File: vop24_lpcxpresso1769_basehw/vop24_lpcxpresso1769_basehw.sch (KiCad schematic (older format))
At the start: 33 parts

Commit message: Esquematico:    - se paso el circuito de fuentes a una hoja aparte    - falta pasar todas las demas a hojas separadas    - terminar conexiones del ads    - poner desacoples de alimentacion para cada IC    - ver como agregar texto para las recomendaciones de ruteo
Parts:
- removed C? (x4): C_Small, symbol C_Small
- removed D? (x2): LED_Small, symbol LED_Small
- removed J?: Conn_01x02, symbol Conn_01x02
- removed R? (x4): R_Small, symbol R_Small
- removed U? (x2): MCP1700T-3302E_TT, digikey-footprints:SOT-23-3, symbol MCP1700T-3302E_TT
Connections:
- net labels removed: VBAT, VREFN
- wire segments 124 -> 101

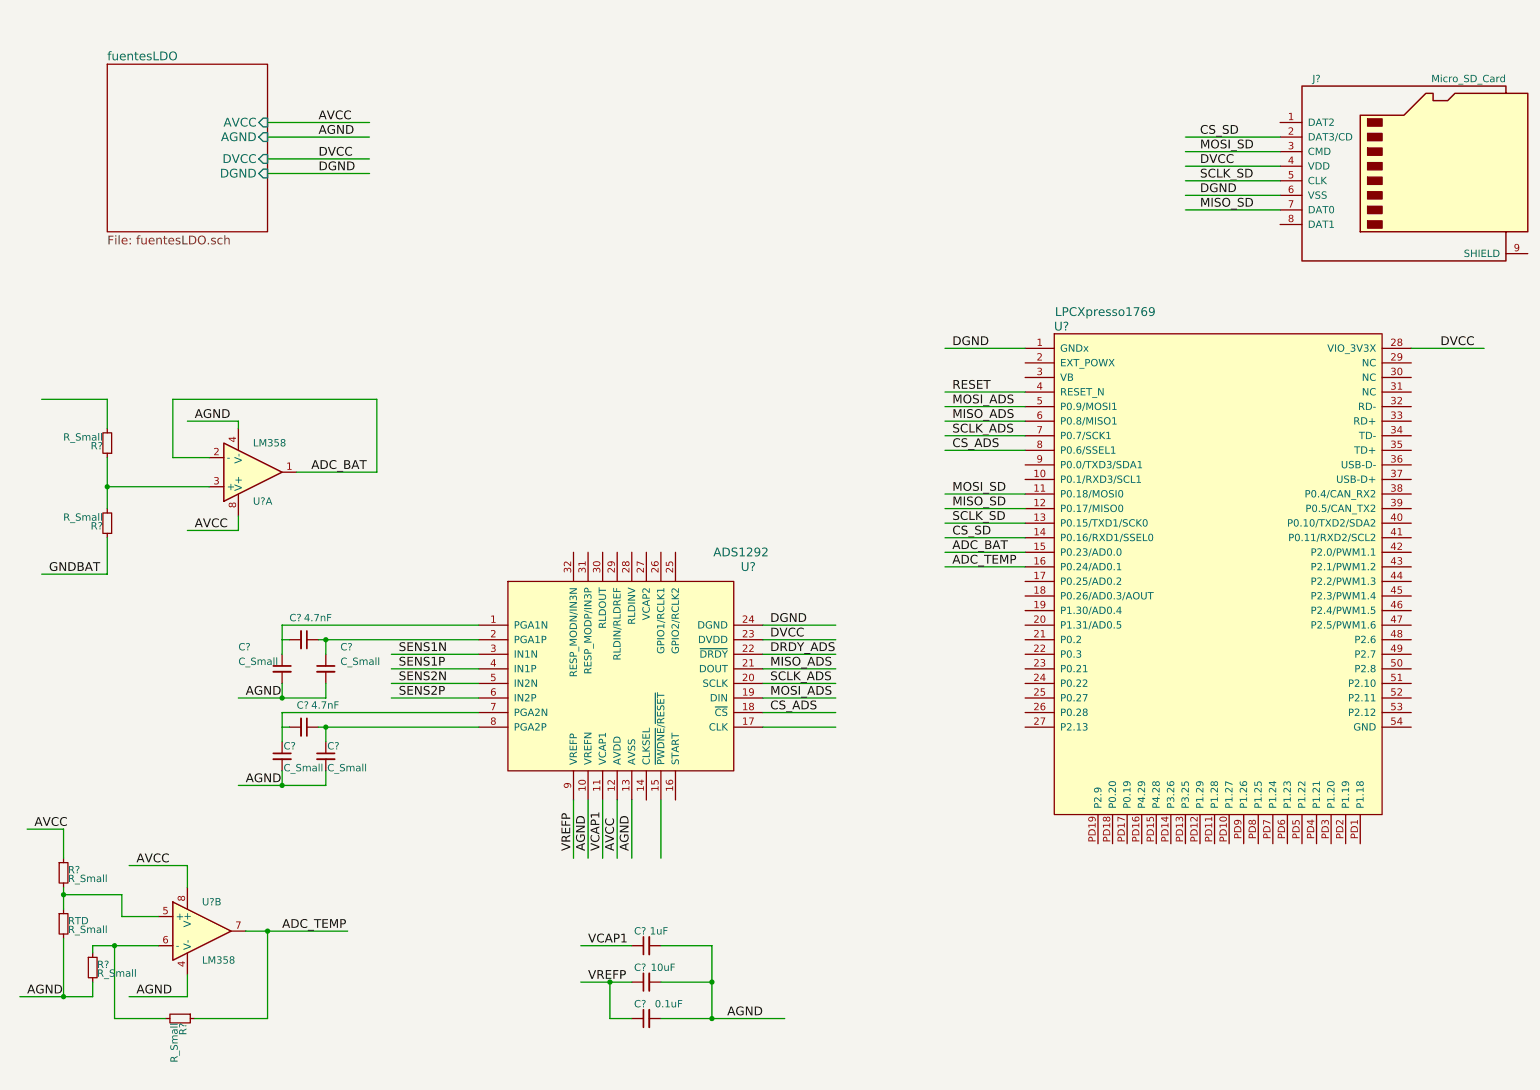
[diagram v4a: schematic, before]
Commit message: Esquematico: agregados hojas separadas de entradas analogicas terminadas y ads1292 sin terminar
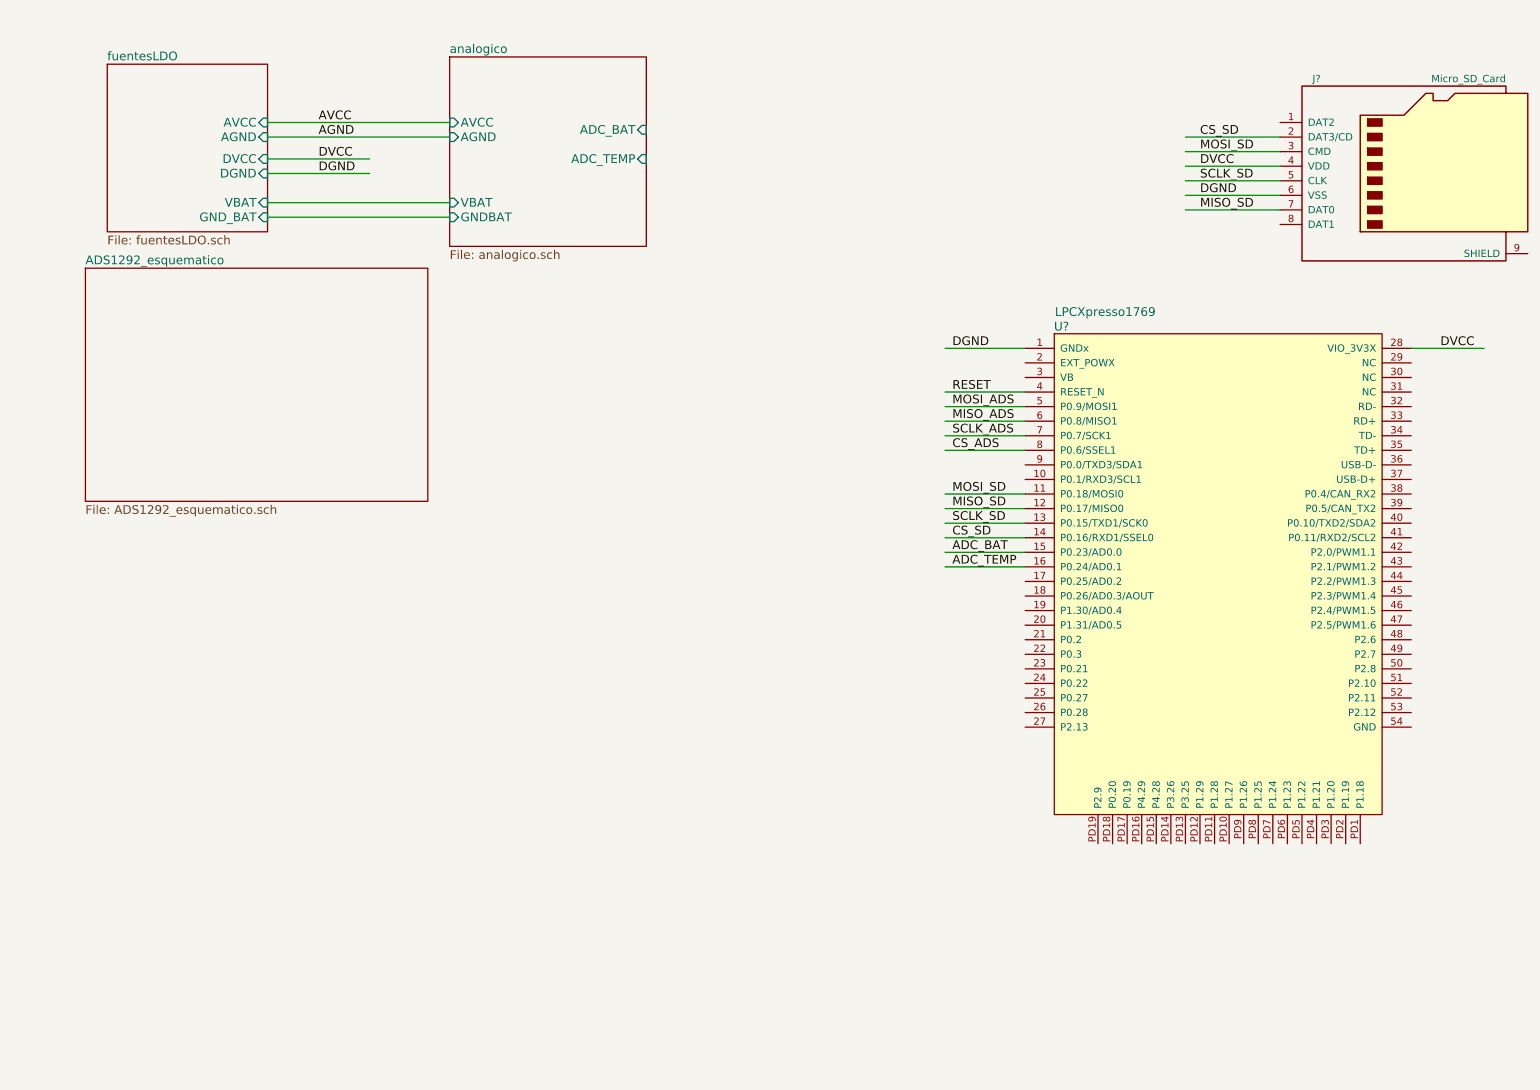
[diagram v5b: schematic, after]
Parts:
- removed C? (x4): C_Small, symbol C_Small
- removed C? (x2): 4.7nF, symbol C_Small
- removed C?: 1uF, symbol C_Small
- removed C?: 10uF, symbol C_Small
- removed C?: 0.1uF, symbol C_Small
- removed R? (x5), RTD: R_Small, symbol R_Small
- removed U? (x2): LM358, symbol LM358
- removed U?: ADS1292, symbol ADS1292
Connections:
- net labels removed: DRDY_ADS, GNDBAT, SENS1N, SENS1P, SENS2N, SENS2P, VCAP1, VREFP
- wire segments 101 -> 25

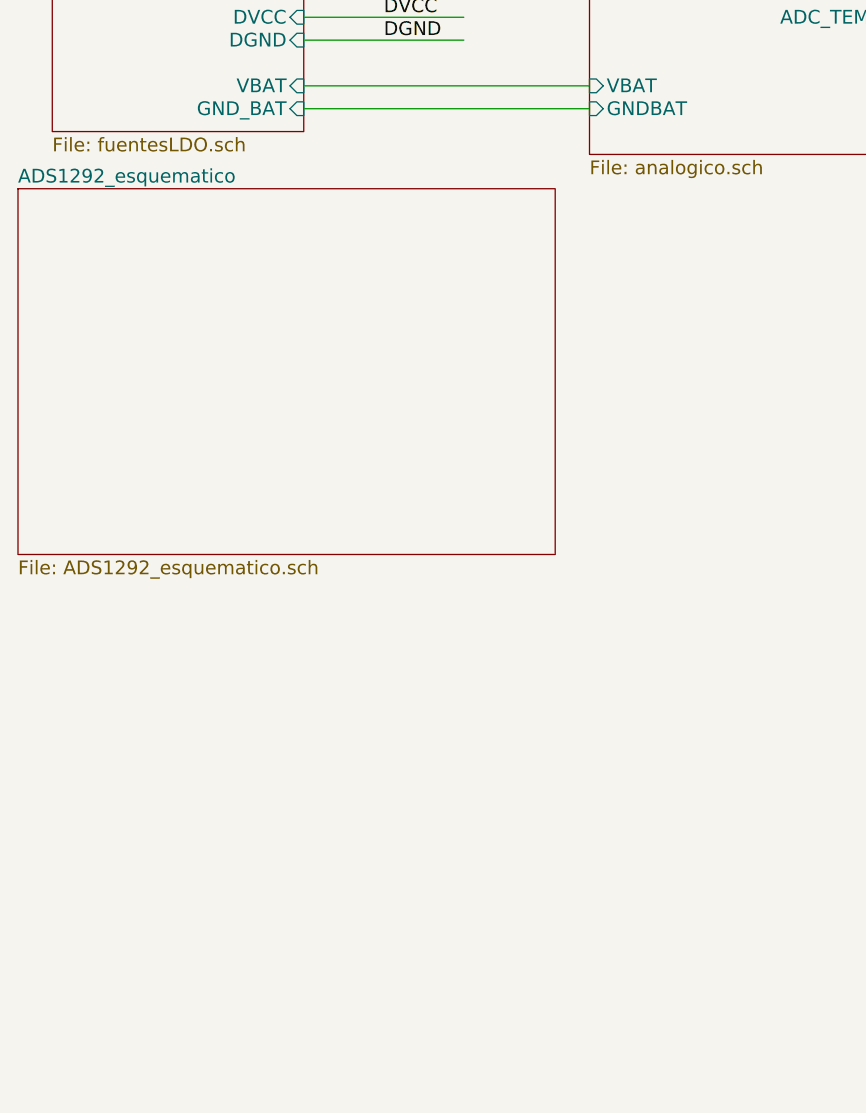
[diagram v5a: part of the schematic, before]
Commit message: Esquematico:    - terminar conexiones de ads: revisar slau387.pdf para conexiones de caps y bobinas    - ver slau387.pdf para medicion de fuente y conexion usb
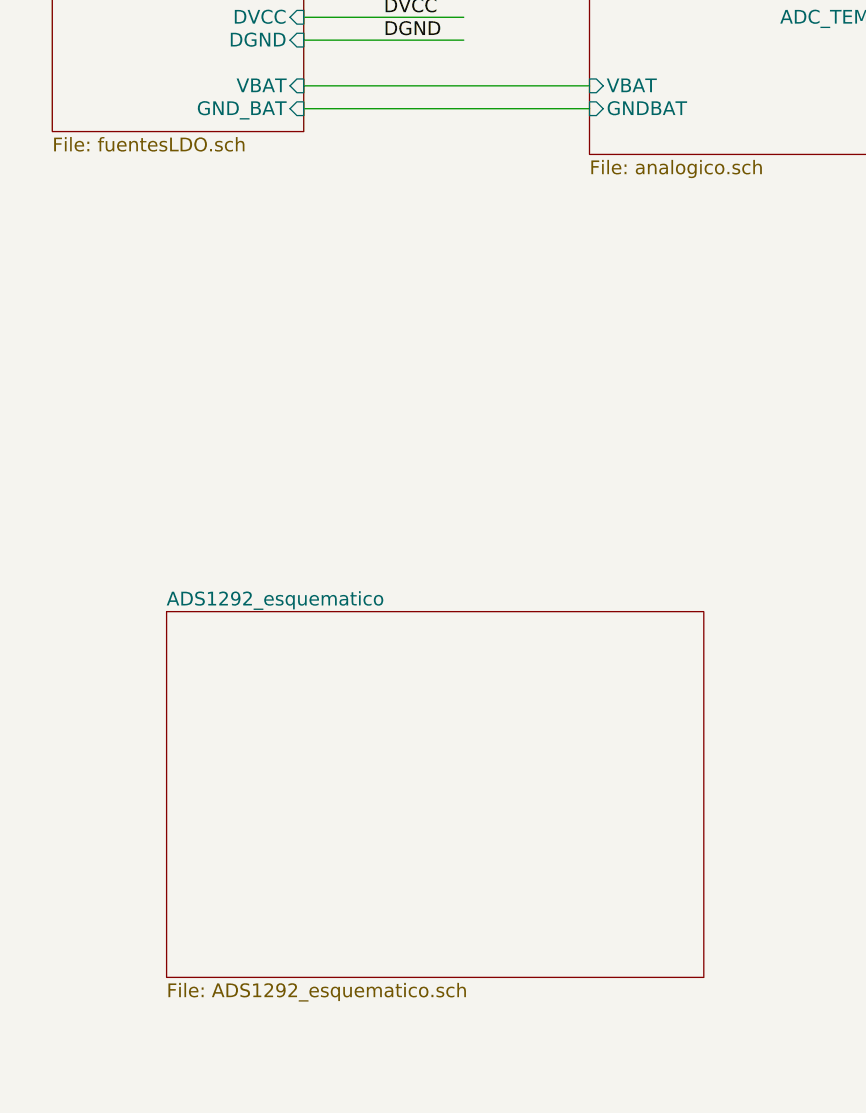
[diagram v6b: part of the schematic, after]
